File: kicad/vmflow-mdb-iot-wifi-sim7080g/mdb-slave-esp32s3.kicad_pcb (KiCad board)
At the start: 2 copper layers, 66.4 x 41 mm, 40 parts, among them J1 MDB_Connector, J2 USB_C_Receptacle_USB2.0_16P, J3 Conn_02x11_Odd_Even, J4 JAE_SIM_Card_SF72S006, SW1 SW_Push, U1 TLP785, U2 SIM7080G, U3 ESP32-S3FH4R2, U4 TLP785, U5 LM2594HVM-3.3, Y1 Crystal_GND24

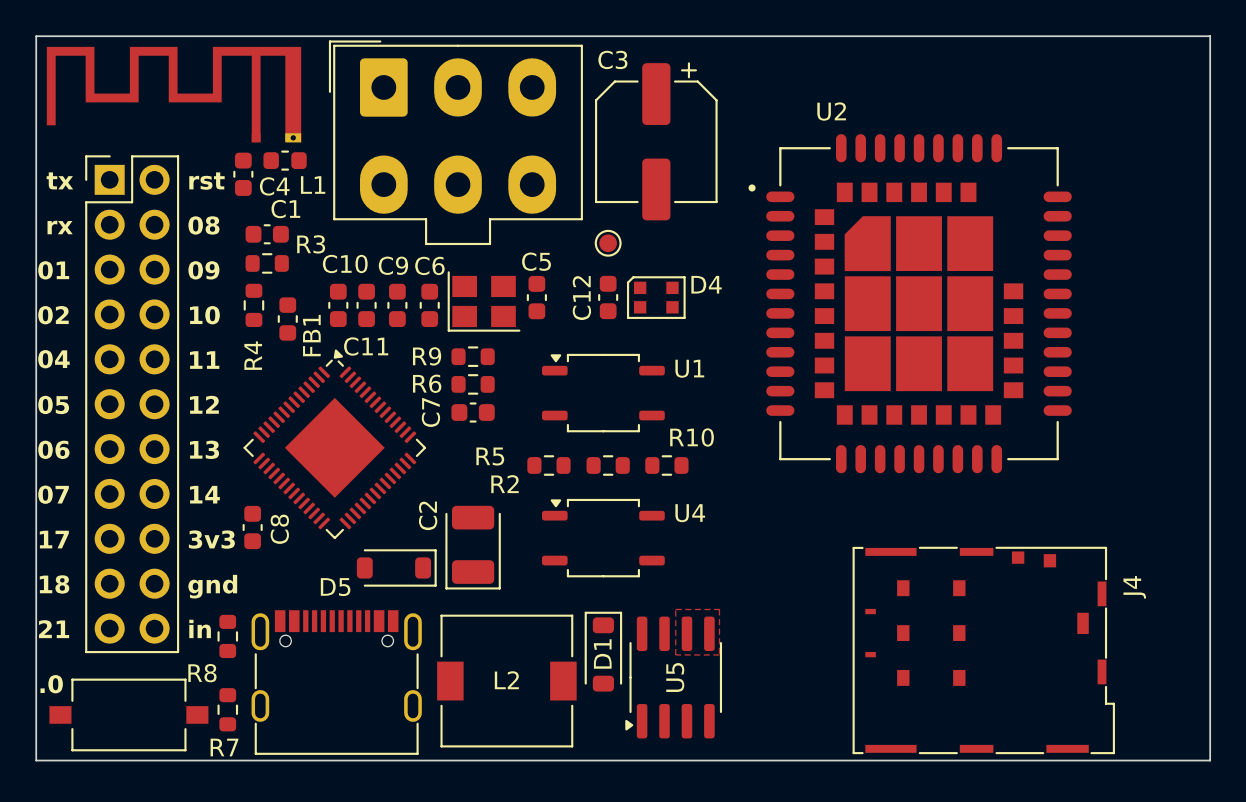
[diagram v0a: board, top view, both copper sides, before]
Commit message: Connecting sim7080G to simcard
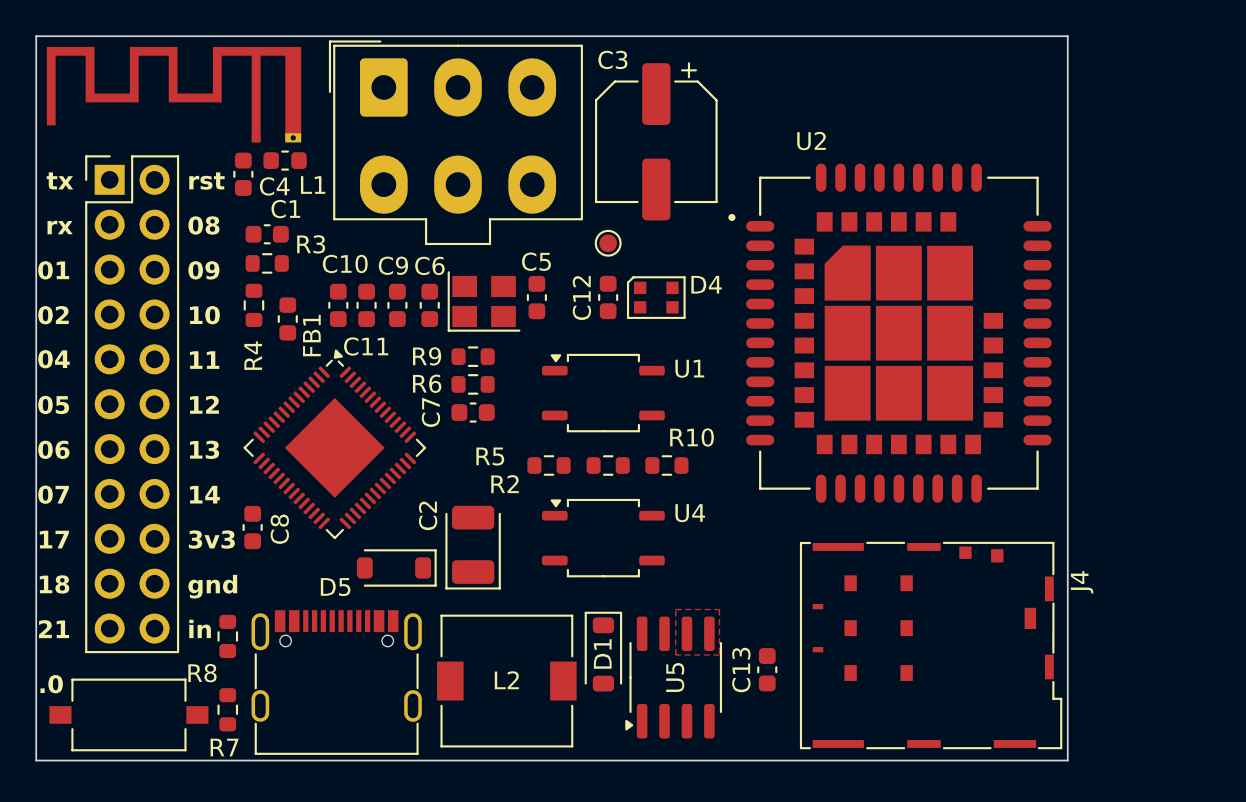
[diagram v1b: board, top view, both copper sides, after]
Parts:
- added C13: 0.1uF, Capacitor_SMD:C_0603_1608Metric, F.Cu at (209.9, 119.0)
- moved J4 2.99 mm to (217.1, 116.6)
- moved U2 2.02 mm to (217.3, 99.9)
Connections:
- J4 pad C1: unconnected-(J4-VCC-PadC1) -> /sim_vdd
- J4 pad C2: unconnected-(J4-RST-PadC2) -> /sim_rst
- J4 pad C3: unconnected-(J4-CLK-PadC3) -> /sim_clk
- J4 pad C5: unconnected-(J4-GND-PadC5) -> GND
- J4 pad C7: unconnected-(J4-I/O-PadC7) -> /sim_data
- J4 pad SH: unconnected-(J4-PadSH) -> GND
- U2 pad 15: unconnected-(U2-SIM_DATA-Pad15) -> /sim_data
- U2 pad 16: unconnected-(U2-SIM_CLK-Pad16) -> /sim_clk
- U2 pad 17: unconnected-(U2-SIM_RST-Pad17) -> /sim_rst
- U2 pad 18: unconnected-(U2-SIM_VDD-Pad18) -> /sim_vdd
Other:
- board size 66.4 x 41 mm -> 58.4 x 41 mm
